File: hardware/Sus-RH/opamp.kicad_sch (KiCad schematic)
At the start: 4 parts, among them U3 Opamp_Dual

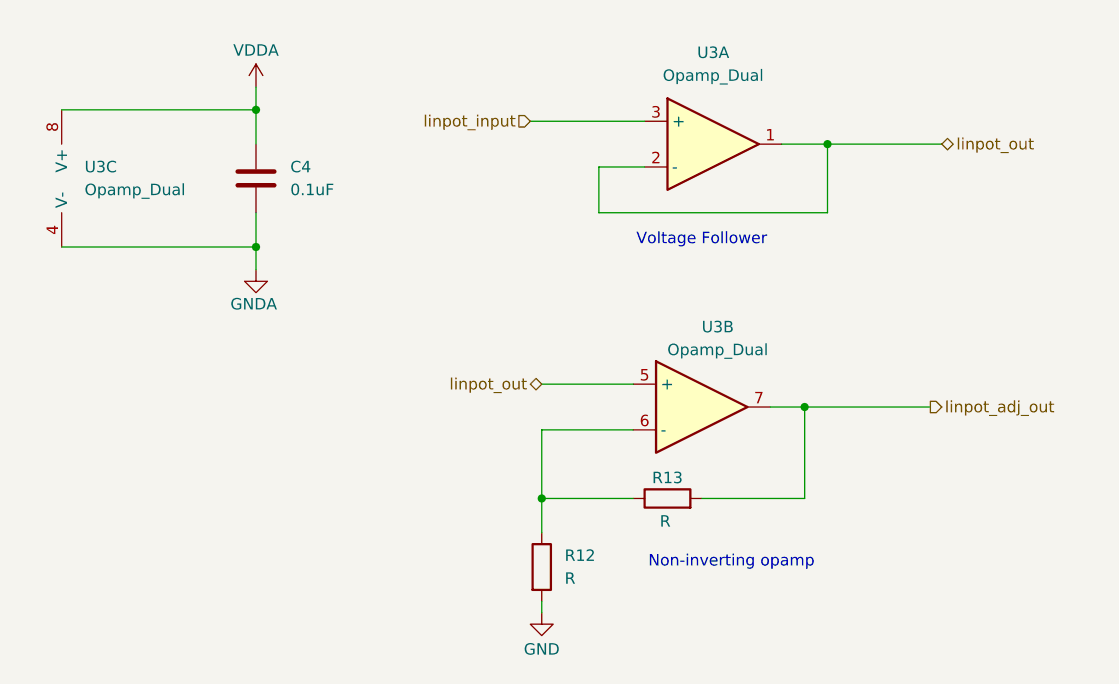
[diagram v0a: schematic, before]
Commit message: finished sch + removed LDO
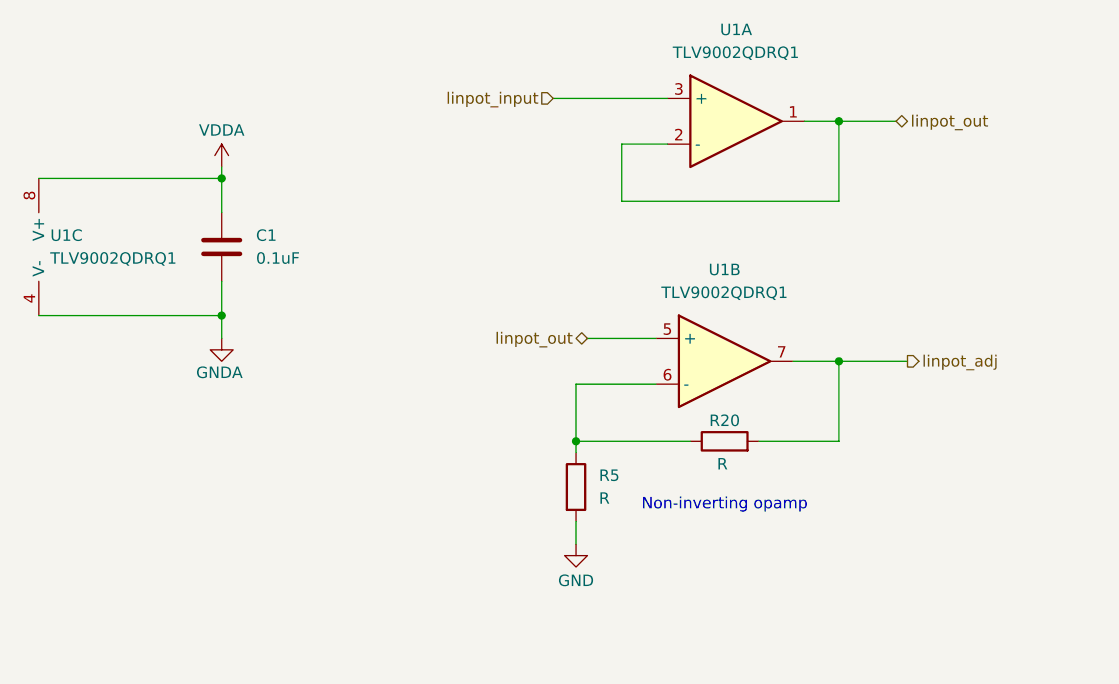
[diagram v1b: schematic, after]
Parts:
- removed C4: 0.1uF, Capacitor_SMD:C_0603_1608Metric_Pad1.08x0.95mm_HandSolder, symbol Device:C
- removed R12, R13: R, symbol Device:R
- removed U3: Opamp_Dual, symbol Device:Opamp_Dual
- added C1: 0.1uF, Capacitor_SMD:C_0603_1608Metric_Pad1.08x0.95mm_HandSolder, symbol Device:C
- added R20, R5: R, symbol Device:R
- added U1: TLV9002QDRQ1, Package_SO:SOIC-8_3.9x4.9mm_P1.27mm, symbol utsvt_misc:TLV9002QDRQ1
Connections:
- net GND: now also R5.2
- net GNDA: now also C1.2, U1.4 (V-)
- net VDDA: now also C1.1, U1.8 (V+)
- net linpot_input: now also U1.3 (+)
- net linpot_out: now also U1.1, U1.2 (-), U1.5 (+)
- new net: R20.1, R5.1, U1.6 (-)
- new net linpot_adj: R20.2, U1.7
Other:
- note removed: "Voltage Follower"

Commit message: removed LDO, added correct cube.
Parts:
- R20, R5: footprint (none) -> Resistor_SMD:R_0603_1608Metric_Pad0.98x0.95mm_HandSolder
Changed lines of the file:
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@@
 			)
 		)
-		(property "Footprint" ""
+		(property "Footprint" "Resistor_SMD:R_0603_1608Metric_Pad0.98x0.95mm_HandSolder"
 			(at 120.65 66.548 90)
 			(effects
@@
 			)
 		)
-		(property "Footprint" ""
+		(property "Footprint" "Resistor_SMD:R_0603_1608Metric_Pad0.98x0.95mm_HandSolder"
 			(at 102.362 69.85 90)
 			(effects

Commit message: op-amp changes
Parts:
- added R12: R, Resistor_SMD:R_0603_1608Metric_Pad0.98x0.95mm_HandSolder, symbol Device:R
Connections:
- net VDDA: now also R12.1
- net at R20.1, R5.1, U1.6 (-): now also R12.2
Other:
- note added: "Both linpot_out and linpot_adj are sent to mcu so if we decide we don't need to perform an offset + amplify, we can just measure linpot_out."
- note removed: "Non-inverting opamp"
- moved on the sheet: R20, R5, U1B
